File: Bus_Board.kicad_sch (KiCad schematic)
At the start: 44 parts, among them J1 +5V, J10 Conn_02x05_Odd_Even, J11 Conn_02x08_Odd_Even, J12 Conn_02x05_Odd_Even, J13 Conn_02x08_Odd_Even, J14 Conn_02x05_Odd_Even, J15 Conn_02x08_Odd_Even, J16 Conn_02x05_Odd_Even, J17 Conn_02x08_Odd_Even, J18 Conn_02x05_Odd_Even, J19 Conn_02x08_Odd_Even, J2 +12V, J20 Conn_02x05_Odd_Even, J21 Conn_02x08_Odd_Even, J22 Conn_02x05_Odd_Even, J23 Conn_02x08_Odd_Even, J24 Conn_02x05_Odd_Even, J25 +5V, J26 +12V, J27 GND, J28 -12V, J3 GND, J4 -12V, J5 Conn_02x08_Odd_Even, J6 Conn_02x05_Odd_Even, J7 Conn_02x08_Odd_Even, J8 Conn_02x05_Odd_Even, J9 Conn_02x08_Odd_Even

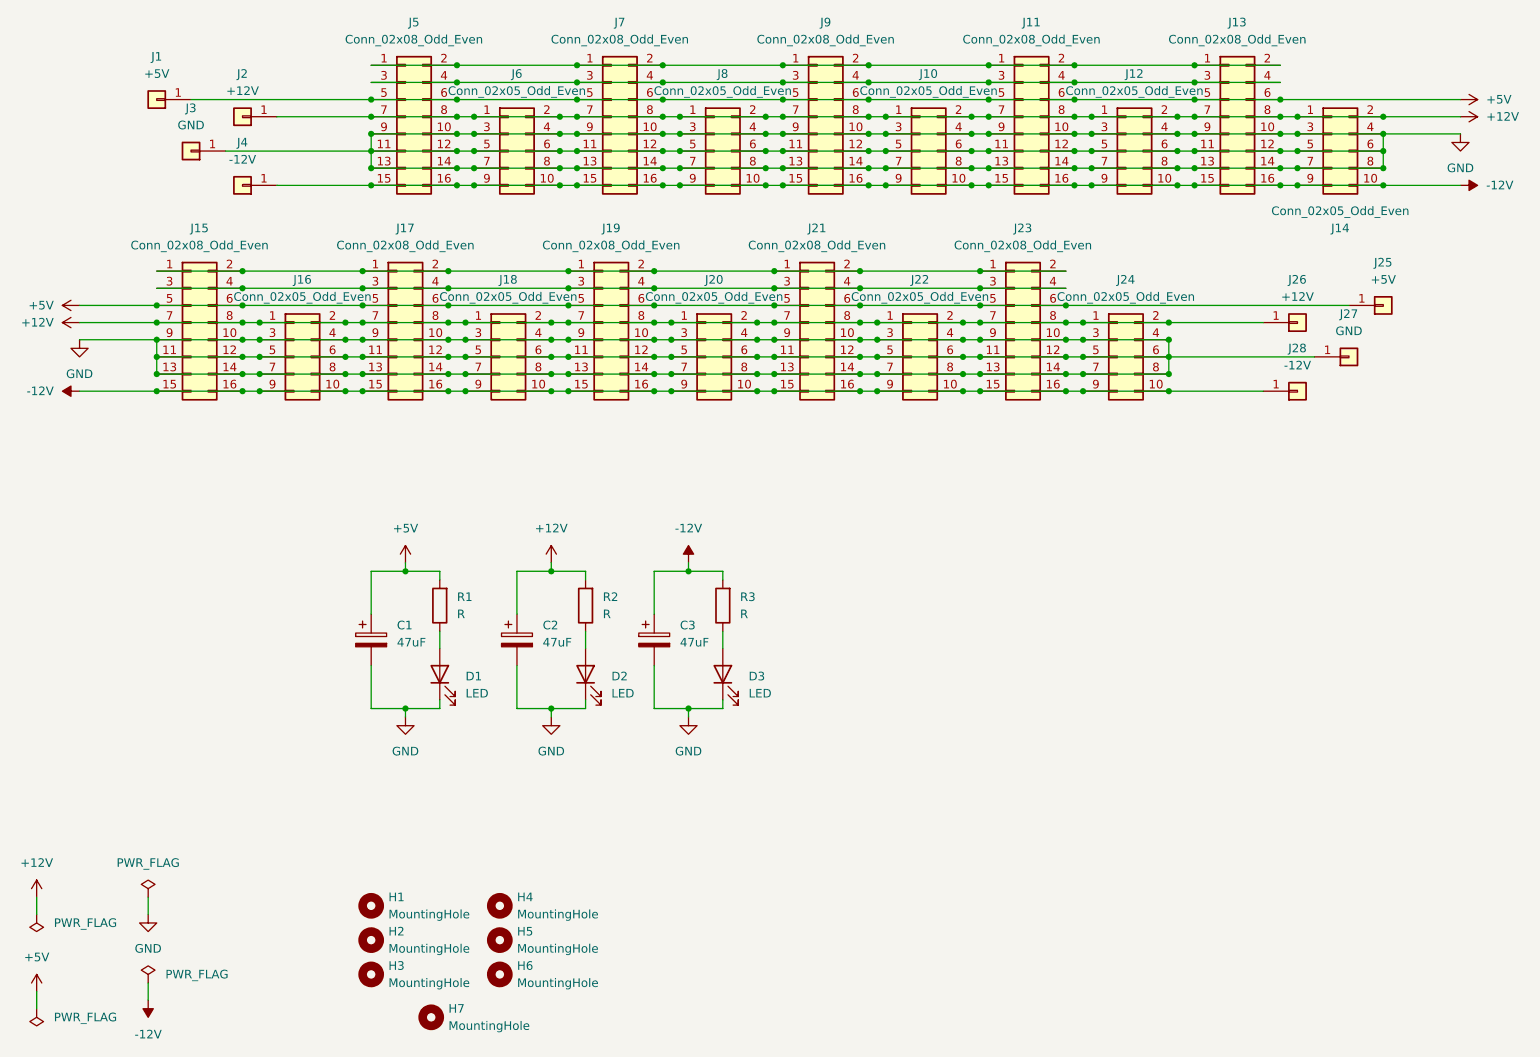
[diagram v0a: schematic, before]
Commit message: Fix orientation of connectors and some other parts
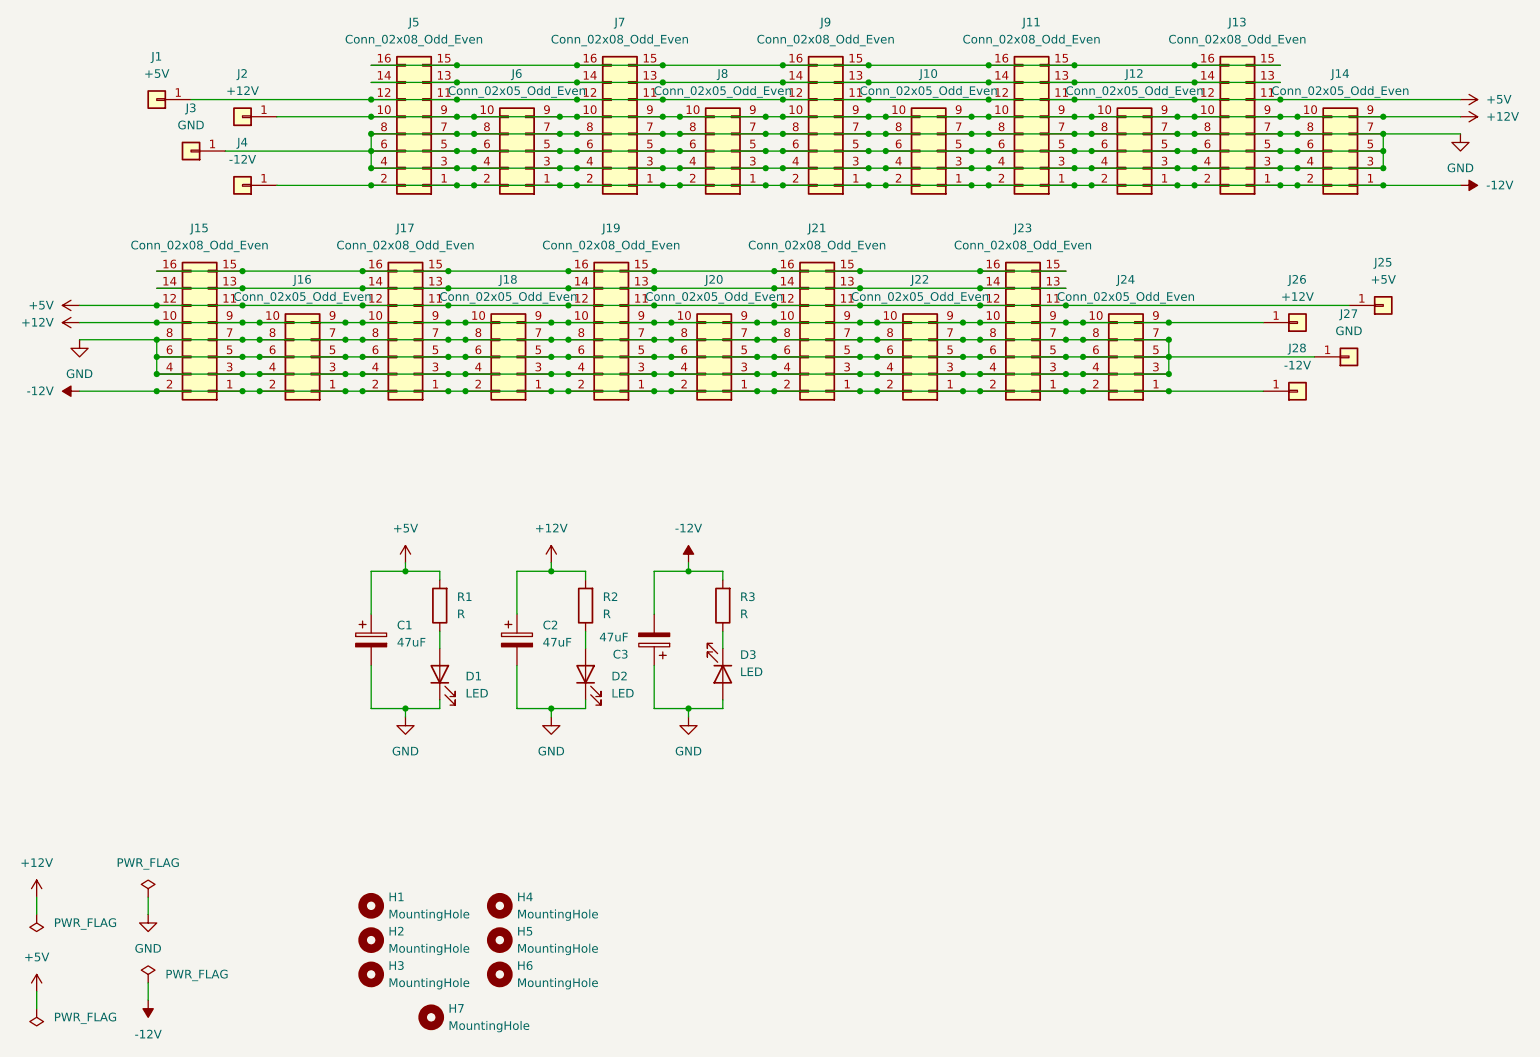
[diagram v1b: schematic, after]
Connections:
- net +12V: now also J10.10 (Pin_10), J10.9 (Pin_9), J11.10 (Pin_10), J11.9 (Pin_9), J12.10 (Pin_10), J12.9 (Pin_9), J13.10 (Pin_10), J13.9 (Pin_9), J14.10 (Pin_10), J14.9 (Pin_9), J15.10 (Pin_10), J15.9 (Pin_9), J16.10 (Pin_10), J16.9 (Pin_9), J17.10 (Pin_10), J17.9 (Pin_9), J18.10 (Pin_10), J18.9 (Pin_9), J19.10 (Pin_10), J19.9 (Pin_9), J20.10 (Pin_10), J20.9 (Pin_9), J21.10 (Pin_10), J21.9 (Pin_9), J22.10 (Pin_10), J22.9 (Pin_9), J23.10 (Pin_10), J23.9 (Pin_9), J24.10 (Pin_10), J24.9 (Pin_9), J5.10 (Pin_10), J5.9 (Pin_9), J6.10 (Pin_10), J6.9 (Pin_9), J7.10 (Pin_10), J7.9 (Pin_9), J8.10 (Pin_10), J8.9 (Pin_9), J9.10 (Pin_10), J9.9 (Pin_9); no longer J10.1 (Pin_1), J10.2 (Pin_2), J11.7 (Pin_7), J11.8 (Pin_8), J12.1 (Pin_1), J12.2 (Pin_2), J13.7 (Pin_7), J13.8 (Pin_8), J14.1 (Pin_1), J14.2 (Pin_2), J15.7 (Pin_7), J15.8 (Pin_8), J16.1 (Pin_1), J16.2 (Pin_2), J17.7 (Pin_7), J17.8 (Pin_8), J18.1 (Pin_1), J18.2 (Pin_2), J19.7 (Pin_7), J19.8 (Pin_8), J20.1 (Pin_1), J20.2 (Pin_2), J21.7 (Pin_7), J21.8 (Pin_8), J22.1 (Pin_1), J22.2 (Pin_2), J23.7 (Pin_7), J23.8 (Pin_8), J24.1 (Pin_1), J24.2 (Pin_2), J5.7 (Pin_7), J5.8 (Pin_8), J6.1 (Pin_1), J6.2 (Pin_2), J7.7 (Pin_7), J7.8 (Pin_8), J8.1 (Pin_1), J8.2 (Pin_2), J9.7 (Pin_7), J9.8 (Pin_8)
- net +5V: now also J11.11 (Pin_11), J11.12 (Pin_12), J13.11 (Pin_11), J13.12 (Pin_12), J15.11 (Pin_11), J15.12 (Pin_12), J17.11 (Pin_11), J17.12 (Pin_12), J19.11 (Pin_11), J19.12 (Pin_12), J21.11 (Pin_11), J21.12 (Pin_12), J23.11 (Pin_11), J23.12 (Pin_12), J5.11 (Pin_11), J5.12 (Pin_12), J7.11 (Pin_11), J7.12 (Pin_12), J9.11 (Pin_11), J9.12 (Pin_12); no longer J11.5 (Pin_5), J11.6 (Pin_6), J13.5 (Pin_5), J13.6 (Pin_6), J15.5 (Pin_5), J15.6 (Pin_6), J17.5 (Pin_5), J17.6 (Pin_6), J19.5 (Pin_5), J19.6 (Pin_6), J21.5 (Pin_5), J21.6 (Pin_6), J23.5 (Pin_5), J23.6 (Pin_6), J5.5 (Pin_5), J5.6 (Pin_6), J7.5 (Pin_5), J7.6 (Pin_6), J9.5 (Pin_5), J9.6 (Pin_6)
- net -12V: now also C3.2, J10.1 (Pin_1), J10.2 (Pin_2), J11.1 (Pin_1), J11.2 (Pin_2), J12.1 (Pin_1), J12.2 (Pin_2), J13.1 (Pin_1), J13.2 (Pin_2), J14.1 (Pin_1), J14.2 (Pin_2), J15.1 (Pin_1), J15.2 (Pin_2), J16.1 (Pin_1), J16.2 (Pin_2), J17.1 (Pin_1), J17.2 (Pin_2), J18.1 (Pin_1), J18.2 (Pin_2), J19.1 (Pin_1), J19.2 (Pin_2), J20.1 (Pin_1), J20.2 (Pin_2), J21.1 (Pin_1), J21.2 (Pin_2), J22.1 (Pin_1), J22.2 (Pin_2), J23.1 (Pin_1), J23.2 (Pin_2), J24.1 (Pin_1), J24.2 (Pin_2), J5.1 (Pin_1), J5.2 (Pin_2), J6.1 (Pin_1), J6.2 (Pin_2), J7.1 (Pin_1), J7.2 (Pin_2), J8.1 (Pin_1), J8.2 (Pin_2), J9.1 (Pin_1), J9.2 (Pin_2); no longer C3.1, J10.10 (Pin_10), J10.9 (Pin_9), J11.15 (Pin_15), J11.16 (Pin_16), J12.10 (Pin_10), J12.9 (Pin_9), J13.15 (Pin_15), J13.16 (Pin_16), J14.10 (Pin_10), J14.9 (Pin_9), J15.15 (Pin_15), J15.16 (Pin_16), J16.10 (Pin_10), J16.9 (Pin_9), J17.15 (Pin_15), J17.16 (Pin_16), J18.10 (Pin_10), J18.9 (Pin_9), J19.15 (Pin_15), J19.16 (Pin_16), J20.10 (Pin_10), J20.9 (Pin_9), J21.15 (Pin_15), J21.16 (Pin_16), J22.10 (Pin_10), J22.9 (Pin_9), J23.15 (Pin_15), J23.16 (Pin_16), J24.10 (Pin_10), J24.9 (Pin_9), J5.15 (Pin_15), J5.16 (Pin_16), J6.10 (Pin_10), J6.9 (Pin_9), J7.15 (Pin_15), J7.16 (Pin_16), J8.10 (Pin_10), J8.9 (Pin_9), J9.15 (Pin_15), J9.16 (Pin_16)
- net GND: now also C3.1, D3.2 (A), J11.3 (Pin_3), J11.4 (Pin_4), J11.5 (Pin_5), J11.6 (Pin_6), J11.7 (Pin_7), J11.8 (Pin_8), J13.3 (Pin_3), J13.4 (Pin_4), J13.5 (Pin_5), J13.6 (Pin_6), J13.7 (Pin_7), J13.8 (Pin_8), J15.3 (Pin_3), J15.4 (Pin_4), J15.5 (Pin_5), J15.6 (Pin_6), J15.7 (Pin_7), J15.8 (Pin_8), J17.3 (Pin_3), J17.4 (Pin_4), J17.5 (Pin_5), J17.6 (Pin_6), J17.7 (Pin_7), J17.8 (Pin_8), J19.3 (Pin_3), J19.4 (Pin_4), J19.5 (Pin_5), J19.6 (Pin_6), J19.7 (Pin_7), J19.8 (Pin_8), J21.3 (Pin_3), J21.4 (Pin_4), J21.5 (Pin_5), J21.6 (Pin_6), J21.7 (Pin_7), J21.8 (Pin_8), J23.3 (Pin_3), J23.4 (Pin_4), J23.5 (Pin_5), J23.6 (Pin_6), J23.7 (Pin_7), J23.8 (Pin_8), J5.3 (Pin_3), J5.4 (Pin_4), J5.5 (Pin_5), J5.6 (Pin_6), J5.7 (Pin_7), J5.8 (Pin_8), J7.3 (Pin_3), J7.4 (Pin_4), J7.5 (Pin_5), J7.6 (Pin_6), J7.7 (Pin_7), J7.8 (Pin_8), J9.3 (Pin_3), J9.4 (Pin_4), J9.5 (Pin_5), J9.6 (Pin_6), J9.7 (Pin_7), J9.8 (Pin_8); no longer C3.2, D3.1 (K), J11.10 (Pin_10), J11.11 (Pin_11), J11.12 (Pin_12), J11.13 (Pin_13), J11.14 (Pin_14), J11.9 (Pin_9), J13.10 (Pin_10), J13.11 (Pin_11), J13.12 (Pin_12), J13.13 (Pin_13), J13.14 (Pin_14), J13.9 (Pin_9), J15.10 (Pin_10), J15.11 (Pin_11), J15.12 (Pin_12), J15.13 (Pin_13), J15.14 (Pin_14), J15.9 (Pin_9), J17.10 (Pin_10), J17.11 (Pin_11), J17.12 (Pin_12), J17.13 (Pin_13), J17.14 (Pin_14), J17.9 (Pin_9), J19.10 (Pin_10), J19.11 (Pin_11), J19.12 (Pin_12), J19.13 (Pin_13), J19.14 (Pin_14), J19.9 (Pin_9), J21.10 (Pin_10), J21.11 (Pin_11), J21.12 (Pin_12), J21.13 (Pin_13), J21.14 (Pin_14), J21.9 (Pin_9), J23.10 (Pin_10), J23.11 (Pin_11), J23.12 (Pin_12), J23.13 (Pin_13), J23.14 (Pin_14), J23.9 (Pin_9), J5.10 (Pin_10), J5.11 (Pin_11), J5.12 (Pin_12), J5.13 (Pin_13), J5.14 (Pin_14), J5.9 (Pin_9), J7.10 (Pin_10), J7.11 (Pin_11), J7.12 (Pin_12), J7.13 (Pin_13), J7.14 (Pin_14), J7.9 (Pin_9), J9.10 (Pin_10), J9.11 (Pin_11), J9.12 (Pin_12), J9.13 (Pin_13), J9.14 (Pin_14), J9.9 (Pin_9)
- net at R3.1: now also D3.1 (K); no longer D3.2 (A)
- new net: J15.13 (Pin_13), J15.14 (Pin_14), J17.13 (Pin_13), J17.14 (Pin_14), J19.13 (Pin_13), J19.14 (Pin_14), J21.13 (Pin_13), J21.14 (Pin_14), J23.13 (Pin_13), J23.14 (Pin_14)
- new net: J15.15 (Pin_15), J15.16 (Pin_16), J17.15 (Pin_15), J17.16 (Pin_16), J19.15 (Pin_15), J19.16 (Pin_16), J21.15 (Pin_15), J21.16 (Pin_16), J23.15 (Pin_15), J23.16 (Pin_16)
- new net: J11.13 (Pin_13), J11.14 (Pin_14), J13.13 (Pin_13), J13.14 (Pin_14), J5.13 (Pin_13), J5.14 (Pin_14), J7.13 (Pin_13), J7.14 (Pin_14), J9.13 (Pin_13), J9.14 (Pin_14)
- new net: J11.15 (Pin_15), J11.16 (Pin_16), J13.15 (Pin_15), J13.16 (Pin_16), J5.15 (Pin_15), J5.16 (Pin_16), J7.15 (Pin_15), J7.16 (Pin_16), J9.15 (Pin_15), J9.16 (Pin_16)
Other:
- moved on the sheet: C3, D3, J10, J11, J12, J13, J14, J15, J16, J17, J18, J19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

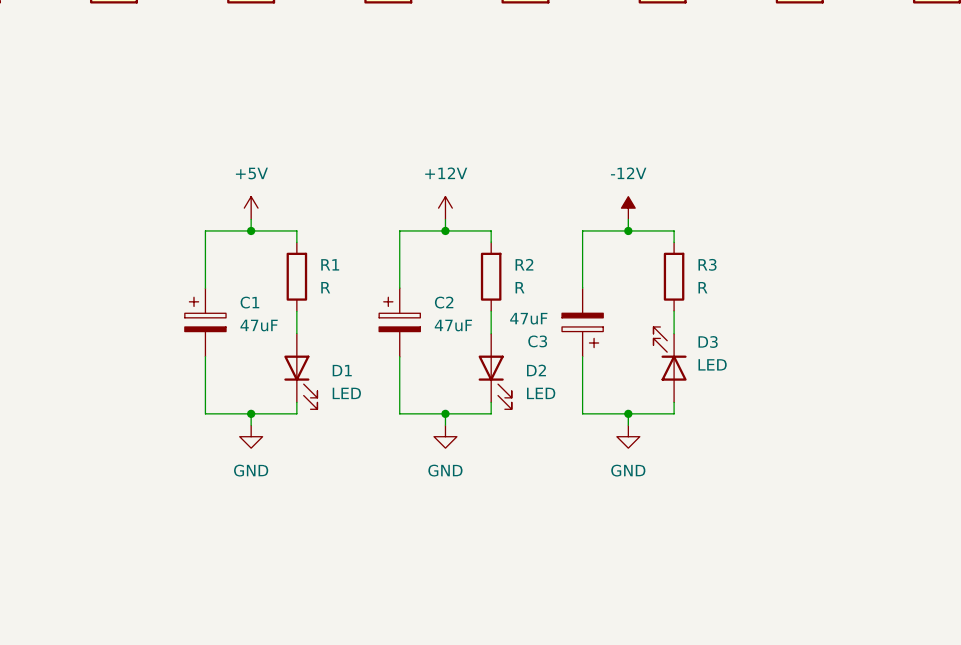
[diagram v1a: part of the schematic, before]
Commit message: Fix Bug, add thermal reliefs to groundplane
Bugfix: reverse polarity of C3 and D3
Add thermal reliefs in ground plane for easier soldering
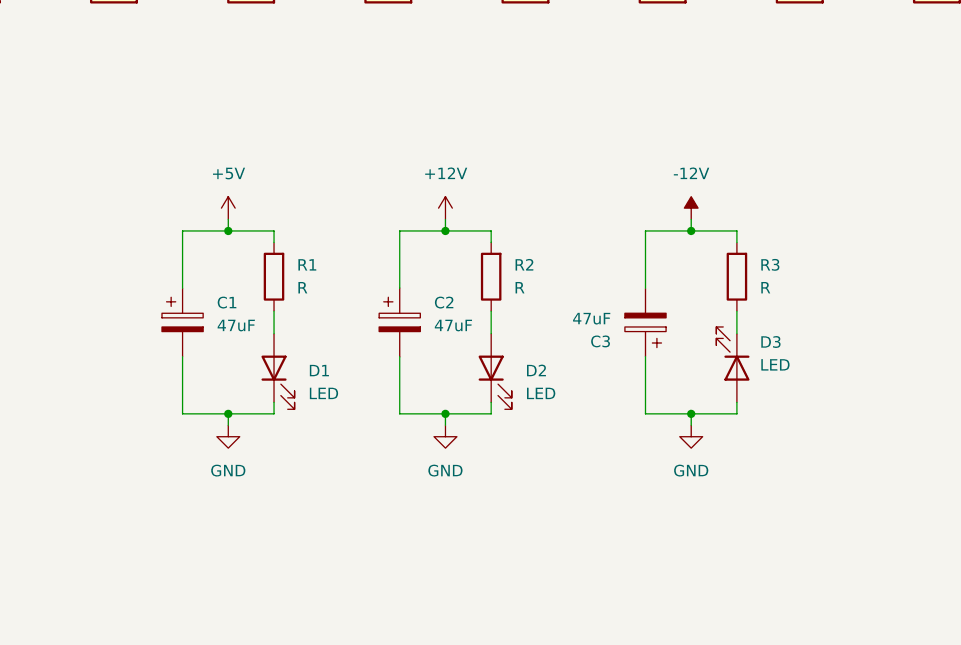
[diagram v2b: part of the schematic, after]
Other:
- company: (none) -> Butch Warns
- title: (none) -> BUS BOARD
- moved on the sheet: C1, C3, D1, D3, R1, R3

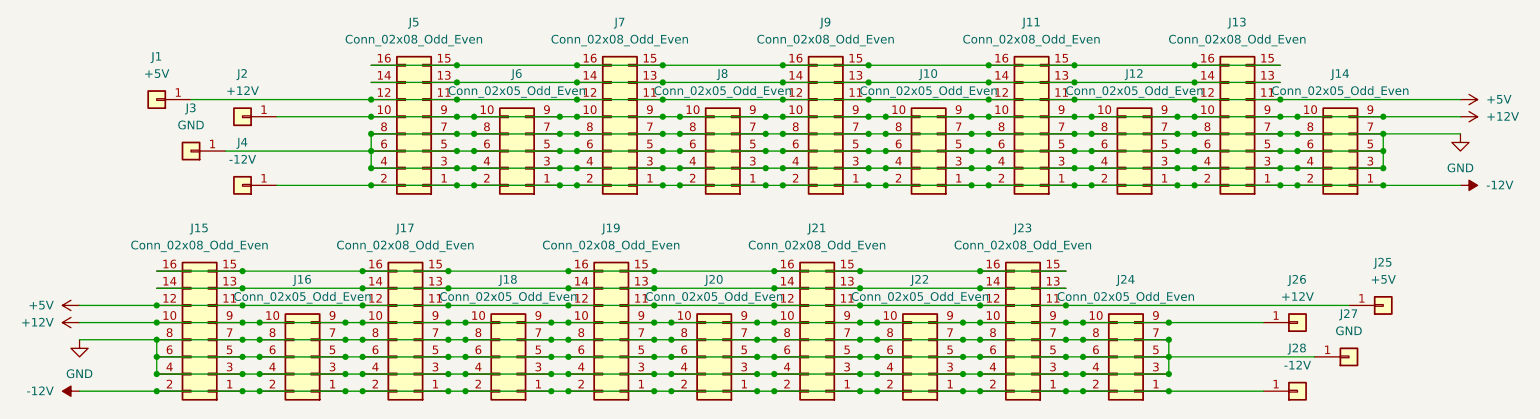
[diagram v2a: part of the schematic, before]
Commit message: Connect CV and GATE lines, add ljcpcb order number
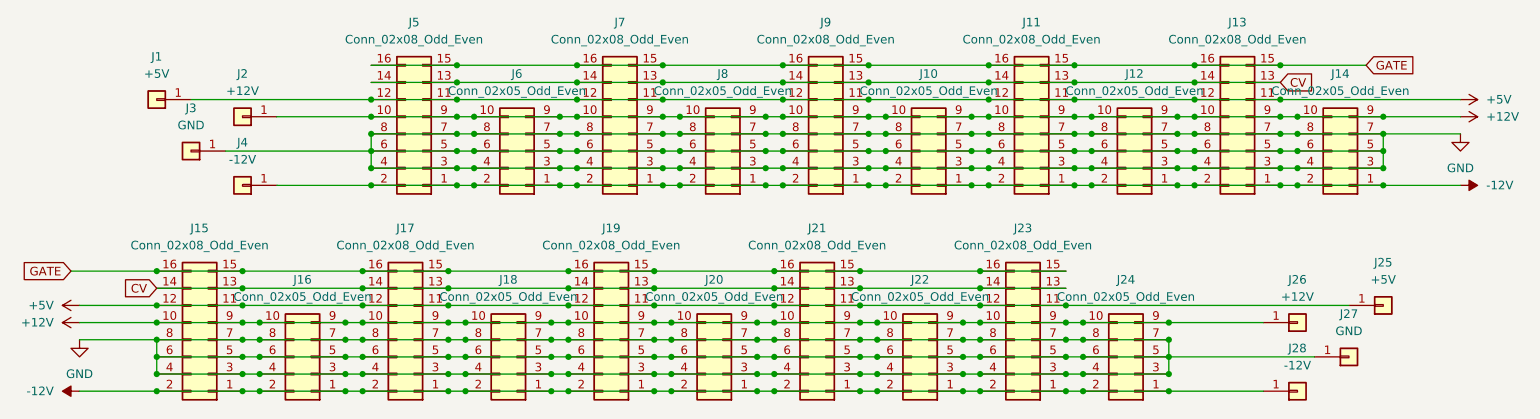
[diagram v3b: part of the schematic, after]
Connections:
- net CV: now reaches J15.13 (Pin_13), J15.14 (Pin_14), J17.13 (Pin_13), J17.14 (Pin_14), J19.13 (Pin_13), J19.14 (Pin_14), J21.13 (Pin_13), J21.14 (Pin_14), J23.13 (Pin_13), J23.14 (Pin_14)
- net CV: now also J11.13 (Pin_13), J11.14 (Pin_14), J13.13 (Pin_13), J13.14 (Pin_14), J5.13 (Pin_13), J5.14 (Pin_14), J7.13 (Pin_13), J7.14 (Pin_14), J9.13 (Pin_13), J9.14 (Pin_14)
- net GATE: now reaches J15.15 (Pin_15), J15.16 (Pin_16), J17.15 (Pin_15), J17.16 (Pin_16), J19.15 (Pin_15), J19.16 (Pin_16), J21.15 (Pin_15), J21.16 (Pin_16), J23.15 (Pin_15), J23.16 (Pin_16)
- net GATE: now also J11.15 (Pin_15), J11.16 (Pin_16), J13.15 (Pin_15), J13.16 (Pin_16), J5.15 (Pin_15), J5.16 (Pin_16), J7.15 (Pin_15), J7.16 (Pin_16), J9.15 (Pin_15), J9.16 (Pin_16)
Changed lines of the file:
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@@
   (junction (at 68.58 71.12) (diameter 0) (color 0 0 0 0)
   )
+  (junction (at 55.88 71.12) (diameter 0) (color 0 0 0 0)
+  )
   (junction (at 193.04 78.74) (diameter 0) (color 0 0 0 0)
   )
@@
   (junction (at 148.59 45.72) (diameter 0) (color 0 0 0 0)
   )
+  (junction (at 222.25 40.64) (diameter 0) (color 0 0 0 0)
+  )
   (junction (at 160.02 83.82) (diameter 0) (color 0 0 0 0)
   )
@@
     (stroke (width 0) (type default) (color 0 0 0 0))
   )
+  (wire (pts (xy 222.25 40.64) (xy 234.95 40.64))
+    (stroke (width 0) (type default) (color 0 0 0 0))
+  )
   (wire (pts (xy 102.87 50.8) (xy 115.57 50.8))
     (stroke (width 0) (type default) (color 0 0 0 0))
@@
     (stroke (width 0) (type default) (color 0 0 0 0))
   )
+  (wire (pts (xy 43.18 71.12) (xy 55.88 71.12))
+    (stroke (width 0) (type default) (color 0 0 0 0))
+  )
   (wire (pts (xy 141.605 114.3) (xy 141.605 115.57))
     (stroke (width 0) (type default) (color 0 0 0 0))
@@
     (stroke (width 0) (type default) (color 0 0 0 0))
   )
+  (global_label "CV" (shape input) (at 222.25 43.18 0) (fields_autoplaced)
+    (effects (font (size 1.27 1.27)) (justify left))
+    (property "Intersheet References" "${INTERSHEET_REFS}" (id 0) (at 227.0217 43.1006 0)
+      (effects (font (size 1.27 1.27)) (justify left) hide)
+    )
+  )
+  (global_label "GATE" (shape input) (at 234.95 40.64 0) (fields_autoplaced)
+    (effects (font (size 1.27 1.27)) (justify left))
+    (property "Intersheet References" "${INTERSHEET_REFS}" (id 0) (at 241.8383 40.5606 0)
+      (effects (font (size 1.27 1.27)) (justify left) hide)
+    )
+  )
+  (global_label "CV" (shape input) (at 55.88 73.66 180) (fields_autoplaced)
+    (effects (font (size 1.27 1.27)) (justify right))
+    (property "Intersheet References" "${INTERSHEET_REFS}" (id 0) (at 51.1083 73.5806 0)
+      (effects (font (size 1.27 1.27)) (justify right) hide)
+    )
+  )
+  (global_label "GATE" (shape input) (at 43.18 71.12 180) (fields_autoplaced)
+    (effects (font (size 1.27 1.27)) (justify right))
+    (property "Intersheet References" "${INTERSHEET_REFS}" (id 0) (at 36.2917 71.0406 0)
+      (effects (font (size 1.27 1.27)) (justify right) hide)
+    )
+  )
   (symbol (lib_id "Mechanical:MountingHole") (at 87.63 175.26 0) (unit 1)

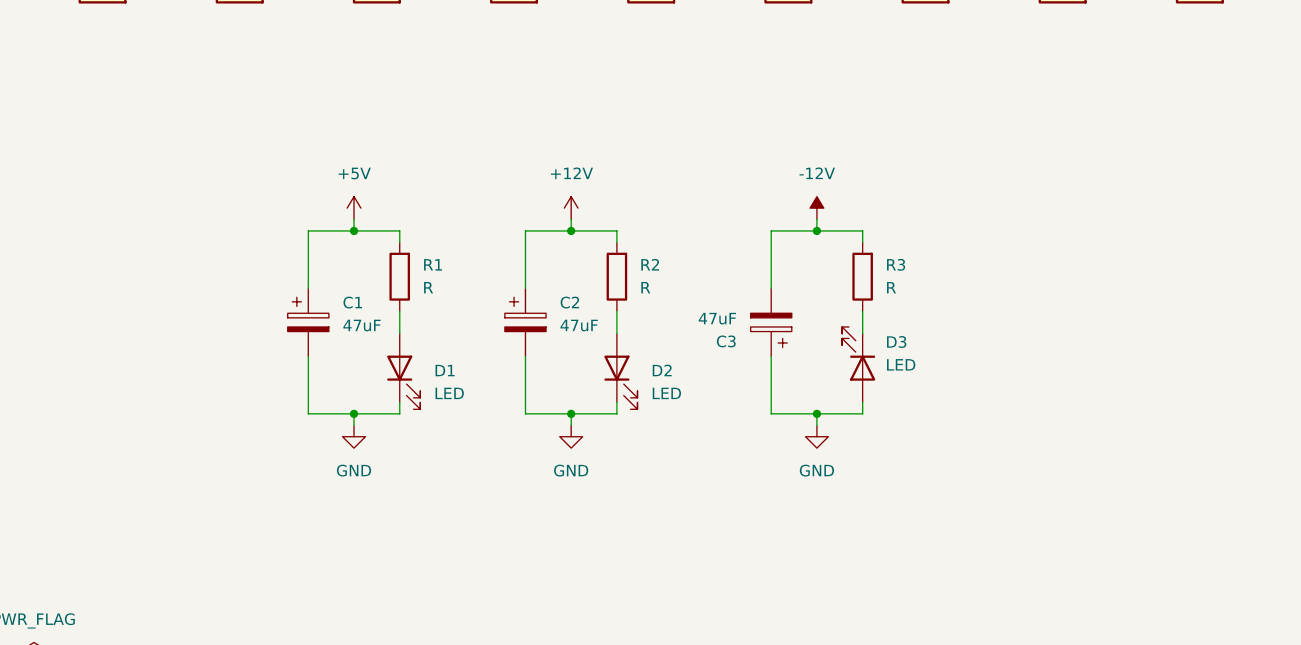
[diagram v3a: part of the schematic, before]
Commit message: Add values to LEDs and resistors
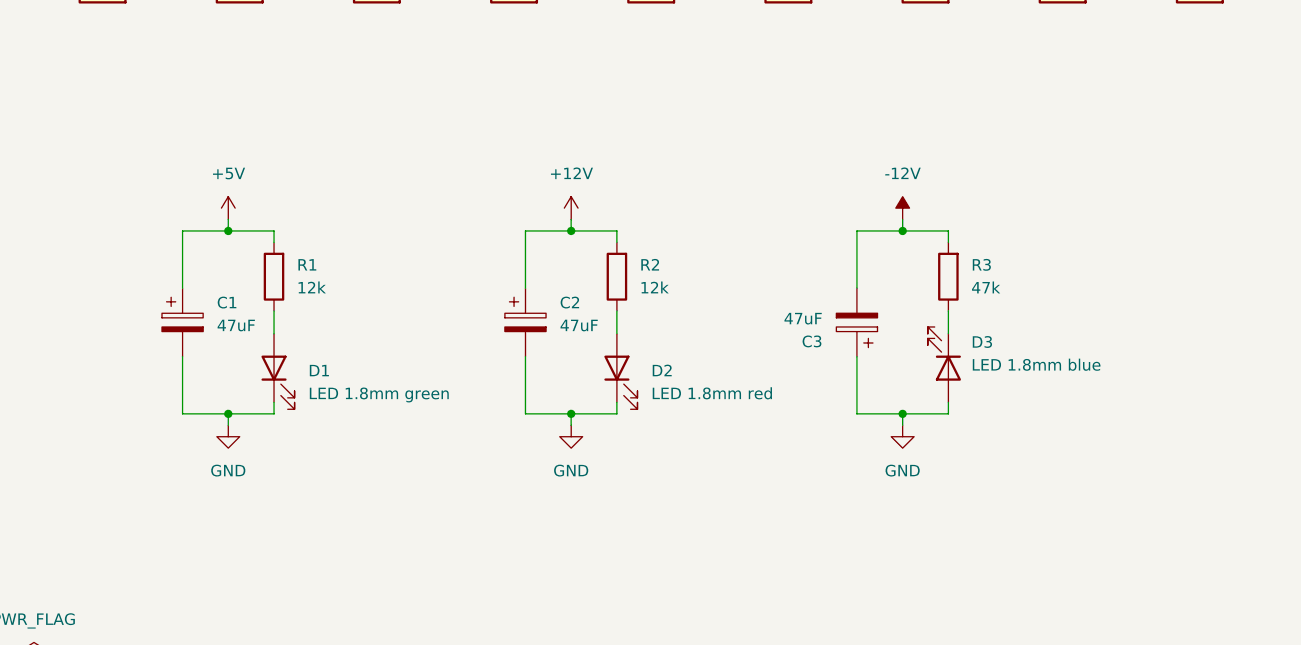
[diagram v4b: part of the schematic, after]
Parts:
- D1: value LED -> LED 1.8mm green
- D2: value LED -> LED 1.8mm red
- D3: value LED -> LED 1.8mm blue
- R1, R2: value R -> 12k
- R3: value R -> 47k
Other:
- moved on the sheet: C1, C3, D1, D3, R1, R3
